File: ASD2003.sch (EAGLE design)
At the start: 22 parts, among them J1 PIN_1X.1"1, J10 PIN_1X.1"1, J11 PIN_1X.1"1, J12 DF12-32-DS, J13 PIN_1X.1"1, J14 PIN_1X.1"1, J15 PIN_1X.1"1, J16 PIN_1X.1"1, J17 PIN_1X.1"1, J18 PIN_1X.1"1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

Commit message: Updated to Rev 3
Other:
- note added: "3"
- note removed: "1"
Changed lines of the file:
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@@
 <?xml version="1.0" encoding="utf-8"?>
 <!DOCTYPE eagle SYSTEM "eagle.dtd">
-<eagle version="6.2">
+<eagle version="6.3">
 <drawing>
 <settings>
@@
 <layer number="106" name="bPlate" color="7" fill="1" visible="yes" active="yes"/>
 <layer number="107" name="Crop" color="7" fill="1" visible="yes" active="yes"/>
+<layer number="108" name="fp8" color="7" fill="1" visible="yes" active="yes"/>
+<layer number="109" name="fp9" color="7" fill="1" visible="yes" active="yes"/>
+<layer number="110" name="fp0" color="7" fill="1" visible="yes" active="yes"/>
+<layer number="111" name="LPC17xx" color="7" fill="1" visible="yes" active="yes"/>
+<layer number="112" name="tSilk" color="7" fill="1" visible="yes" active="yes"/>
 <layer number="116" name="Patch_BOT" color="7" fill="1" visible="yes" active="yes"/>
 <layer number="121" name="_tsilk" color="7" fill="1" visible="yes" active="yes"/>
 <layer number="122" name="_bsilk" color="7" fill="1" visible="yes" active="yes"/>
+<layer number="123" name="tTestmark" color="7" fill="1" visible="yes" active="yes"/>
+<layer number="124" name="bTestmark" color="7" fill="1" visible="yes" active="yes"/>
+<layer number="125" name="_tNames" color="7" fill="1" visible="yes" active="yes"/>
+<layer number="126" name="_bNames" color="7" fill="1" visible="yes" active="yes"/>
+<layer number="127" name="_tValues" color="7" fill="1" visible="yes" active="yes"/>
+<layer number="128" name="_bValues" color="7" fill="1" visible="yes" active="yes"/>
+<layer number="131" name="tAdjust" color="7" fill="1" visible="yes" active="yes"/>
+<layer number="132" name="bAdjust" color="7" fill="1" visible="yes" active="yes"/>
 <layer number="144" name="Drill_legend" color="7" fill="1" visible="yes" active="yes"/>
 <layer number="151" name="HeatSink" color="7" fill="1" visible="yes" active="yes"/>
+<layer number="152" name="_bDocu" color="7" fill="1" visible="yes" active="yes"/>
+<layer number="199" name="Contour" color="7" fill="1" visible="yes" active="yes"/>
 <layer number="200" name="200bmp" color="7" fill="1" visible="yes" active="yes"/>
 <layer number="201" name="201bmp" color="7" fill="1" visible="yes" active="yes"/>
@@
 <layer number="223" name="223bmp" color="7" fill="1" visible="yes" active="yes"/>
 <layer number="224" name="224bmp" color="7" fill="1" visible="yes" active="yes"/>
+<layer number="248" name="Housing" color="7" fill="1" visible="yes" active="yes"/>
+<layer number="249" name="Edge" color="7" fill="1" visible="yes" active="yes"/>
 <layer number="250" name="Descript" color="7" fill="1" visible="yes" active="yes"/>
 <layer number="251" name="SMDround" color="7" fill="1" visible="yes" active="yes"/>
@@
 <text x="340.868" y="17.272" size="3.556" layer="94" font="vector">TinyShield - Proto3</text>
 <text x="327.152" y="6.35" size="3.556" layer="94" font="vector">AS-SCH-ASD2003</text>
-<text x="416.56" y="6.858" size="3.556" layer="94" font="vector">1</text>
+<text x="416.56" y="6.858" size="3.556" layer="94" font="vector">3</text>
 <text x="304.8" y="165.354" size="1.778" layer="91">IOREF</text>
 <text x="45.72" y="35.56" size="3.048" layer="91">Released under the Creative Commons Attribution Share-Alike 3.0 License</text>

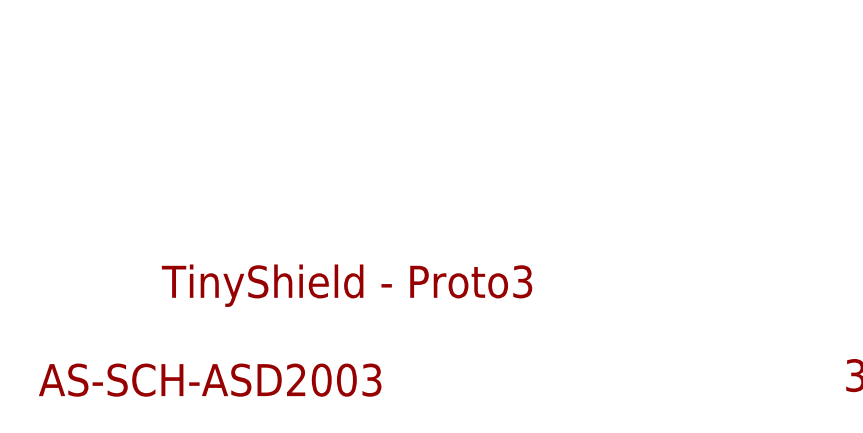
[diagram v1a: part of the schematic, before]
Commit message: Fixed incorrect schematic label
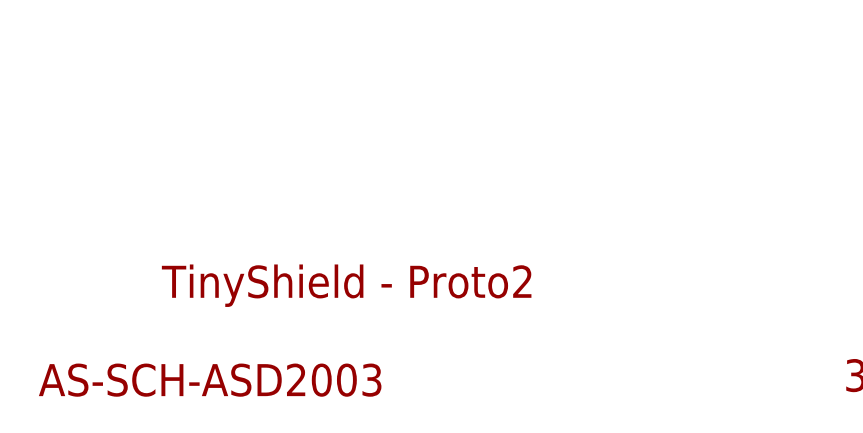
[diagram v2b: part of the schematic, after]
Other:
- note added: "TinyShield - Proto2"
- note removed: "TinyShield - Proto3"
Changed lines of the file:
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@@
 <plain>
 <text x="248.92" y="187.96" size="3.81" layer="94" font="vector">TinyShield Expansion - Bottom</text>
-<text x="340.868" y="17.272" size="3.556" layer="94" font="vector">TinyShield - Proto3</text>
+<text x="340.868" y="17.272" size="3.556" layer="94" font="vector">TinyShield - Proto2</text>
 <text x="327.152" y="6.35" size="3.556" layer="94" font="vector">AS-SCH-ASD2003</text>
 <text x="416.56" y="6.858" size="3.556" layer="94" font="vector">3</text>
